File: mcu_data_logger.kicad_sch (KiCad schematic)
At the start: 25 parts, among them U1 24LC1025, U2 DS1337S_, U3 24LC1025, U4 ATMEGA328P-AU, Y1 32.768 kHz, Y2 16MHz

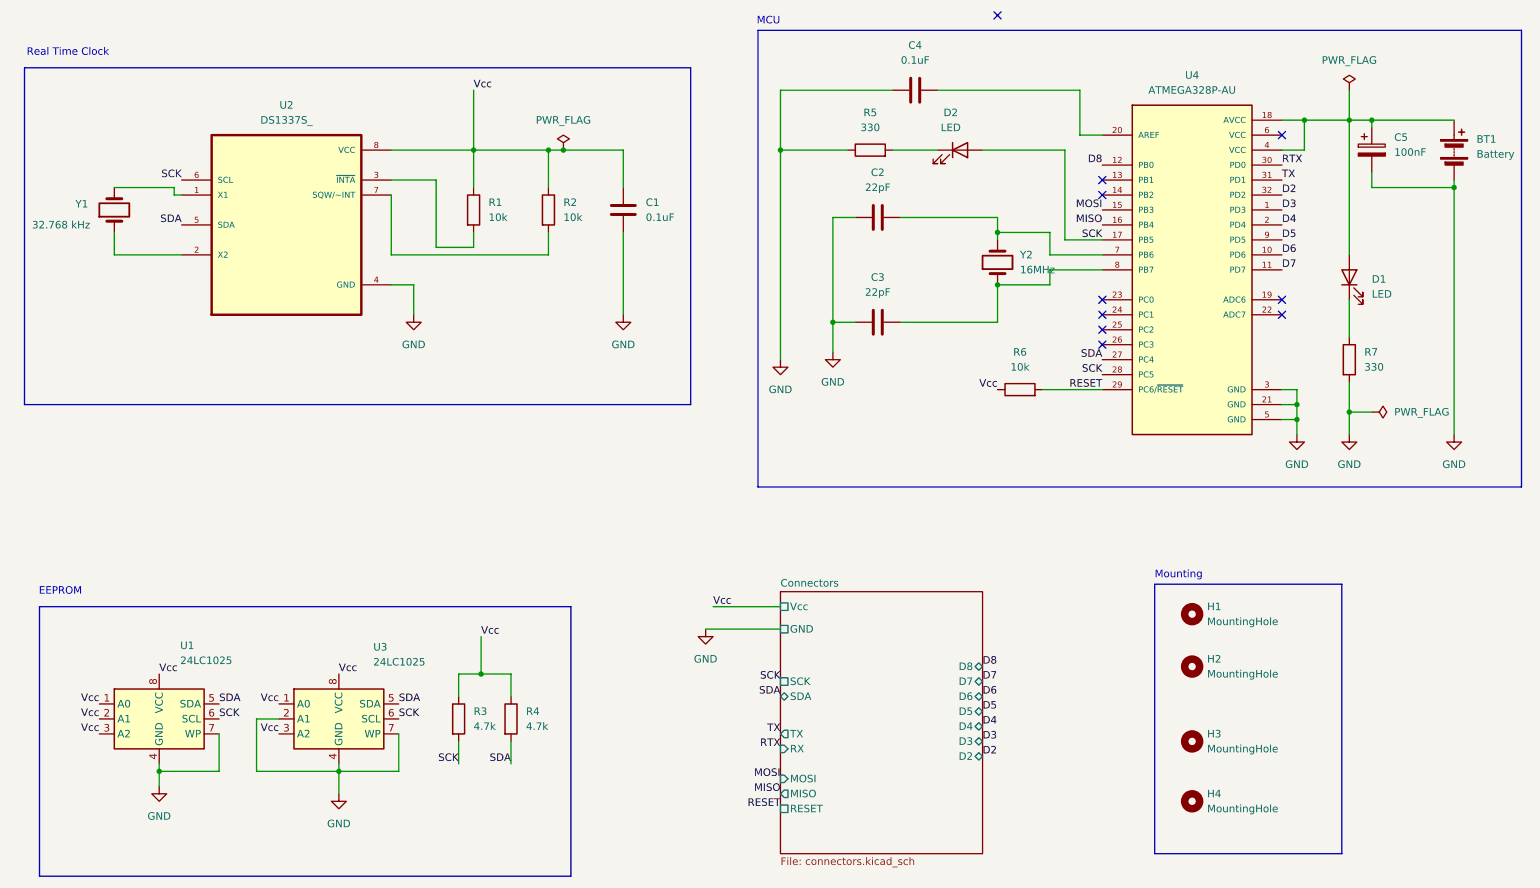
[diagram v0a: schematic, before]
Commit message: renamed RTX label from main sheet to RX
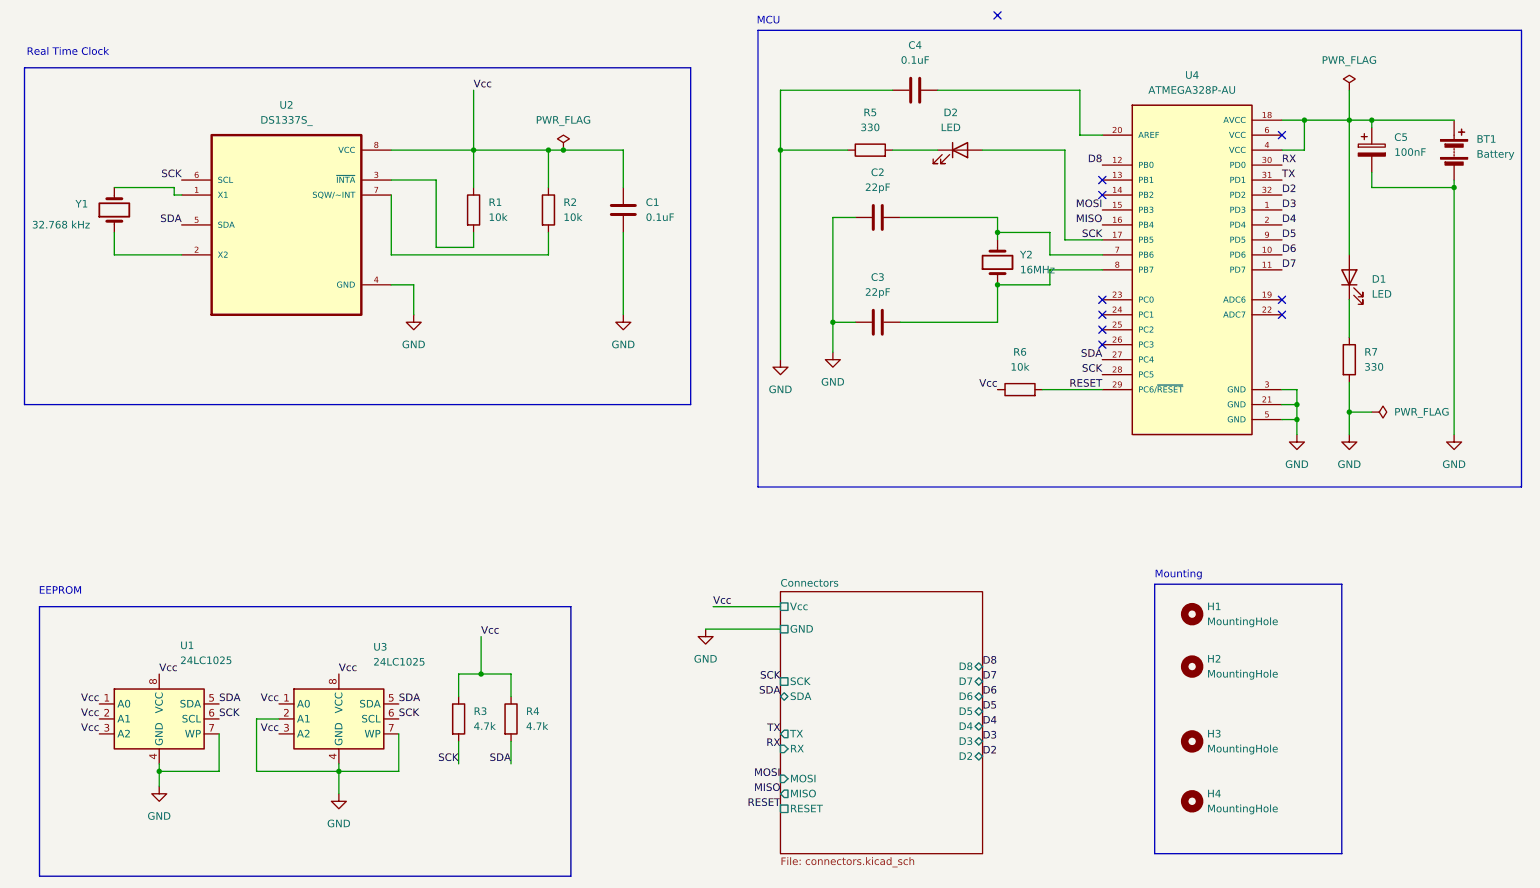
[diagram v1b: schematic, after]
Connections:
- net RTX renamed RX
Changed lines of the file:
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@@
 		)
 	)
-	(label "RTX"
+	(label "RX"
 		(at 157.48 142.24 180)
 		(effects
@@
 		)
 	)
-	(label "RTX"
+	(label "RX"
 		(at 242.57 43.18 0)
 		(effects

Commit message: Partial arrangement of footprints and change of battery component footprint
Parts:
- BT1: footprint Connector_PinHeader_2.54mm:PinHeader_1x02_P2.54mm_Horizontal -> Connector_PinHeader_2.54mm:PinHeader_1x02_P2.54mm_Vertical
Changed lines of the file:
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@@
 			)
 		)
-		(property "Footprint" "Connector_PinHeader_2.54mm:PinHeader_1x02_P2.54mm_Horizontal"
+		(property "Footprint" "Connector_PinHeader_2.54mm:PinHeader_1x02_P2.54mm_Vertical"
 			(at 271.78 39.116 90)
 			(effects

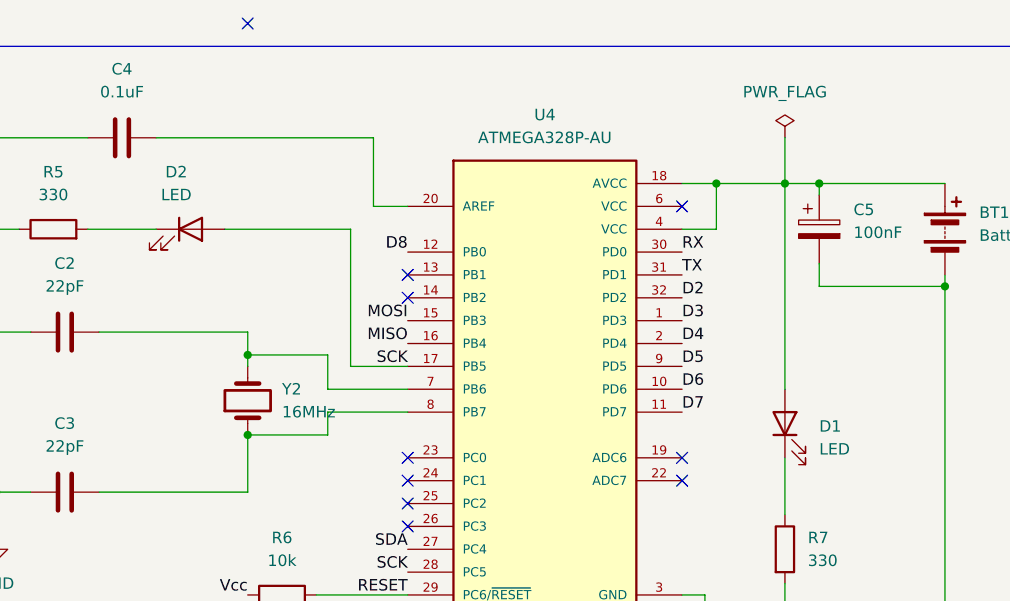
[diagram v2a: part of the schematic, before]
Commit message: swapped D1 and D2 diode references
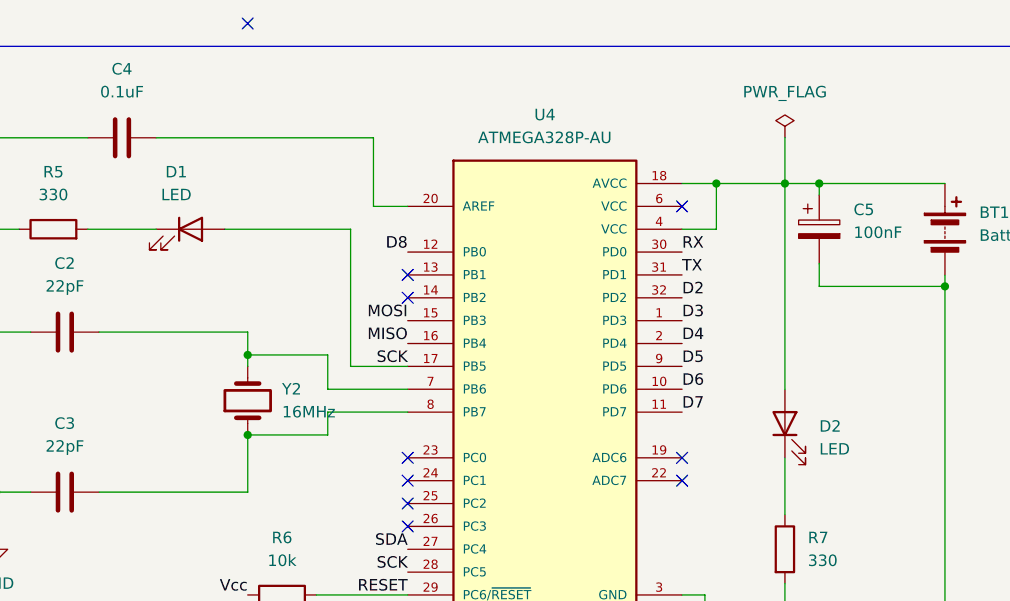
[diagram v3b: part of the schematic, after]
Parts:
- renumbered D2 to D1, D1 to D2
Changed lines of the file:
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@@
 		(dnp no)
 		(fields_autoplaced yes)
-		(property "Reference" "D2"
+		(property "Reference" "D1"
 			(at 186.3725 34.29 0)
 			(effects
@@
 			)
 		)
+		(property "Purpose" ""
+			(at 187.96 40.64 0)
+			(effects
+				(font
+					(size 1.27 1.27)
+				)
+			)
+		)
 		(pin "2"
 		)
@@
 			(project "mcu_data_logger"
 				(path "/8d241645-05dd-4180-8806-a9efe0716d11"
-					(reference "D2")
+					(reference "D1")
 					(unit 1)
 				)
@@
 		(dnp no)
 		(fields_autoplaced yes)
-		(property "Reference" "D1"
+		(property "Reference" "D2"
 			(at 257.81 62.5474 90)
 			(effects
@@
 			)
 		)
+		(property "Purpose" ""
+			(at 254 62.23 0)
+			(effects
+				(font
+					(size 1.27 1.27)
+				)
+			)
+		)
 		(pin "2"
 		)
@@
 			(project ""
 				(path "/8d241645-05dd-4180-8806-a9efe0716d11"
-					(reference "D1")
-					(unit 1)
-				)
+					(reference "D2")
+					(unit 1)
+				)

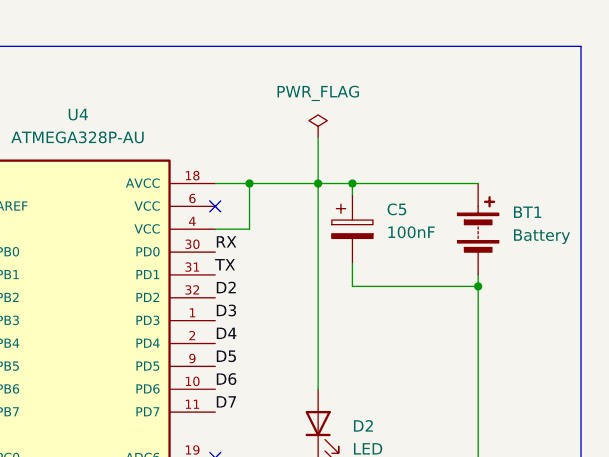
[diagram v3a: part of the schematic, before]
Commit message: assigned the Vcc net to the BT1 positive terminal in the Schematic Editor which resulted in a lot of bug fixing and rerouting in the PCB Editor
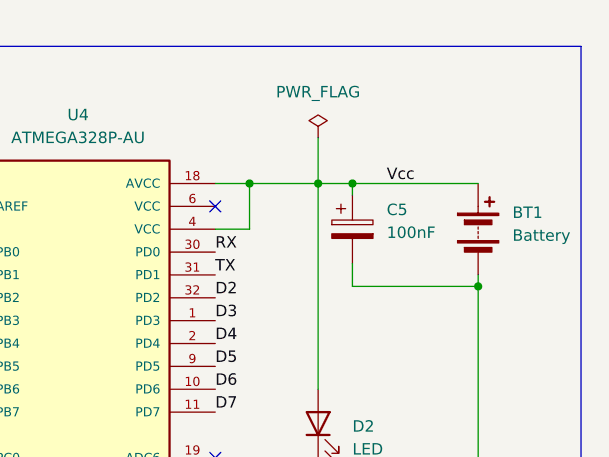
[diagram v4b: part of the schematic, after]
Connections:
- net Vcc: now also BT1.1 (+), C5.1, D2.2 (A), U4.18 (AVCC), U4.4 (VCC)
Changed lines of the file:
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@@
+		)
+	)
+	(label "Vcc"
+		(at 261.62 35.56 0)
+		(effects
+			(font
+				(size 1.27 1.27)
+			)
+			(justify left bottom)
 		)
 	)

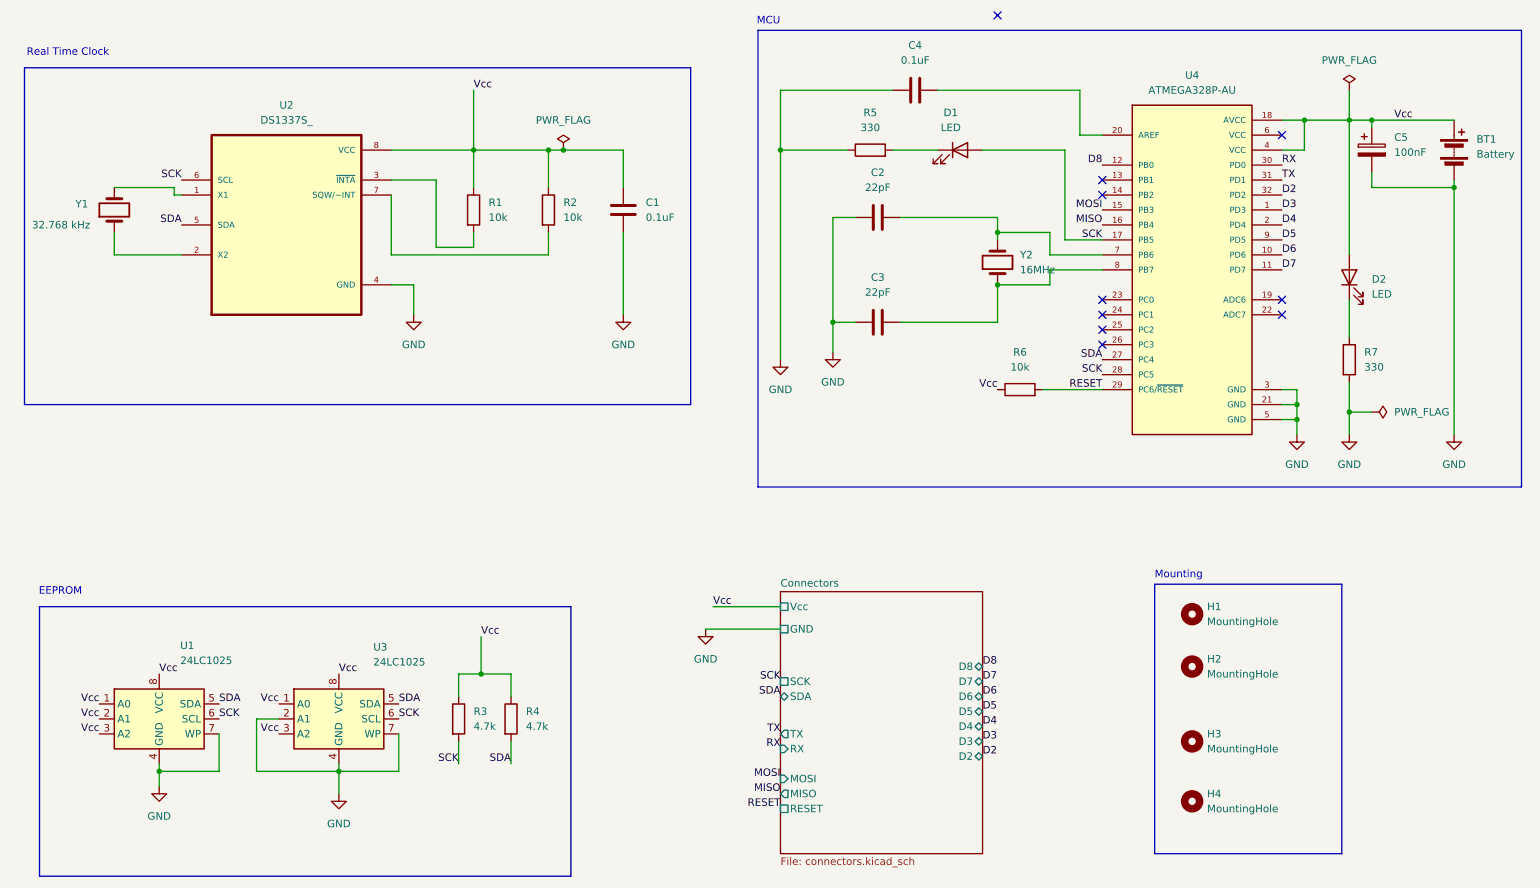
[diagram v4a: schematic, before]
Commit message: fixed net label bugs for i2c and icsp clock signal ports in the schematics
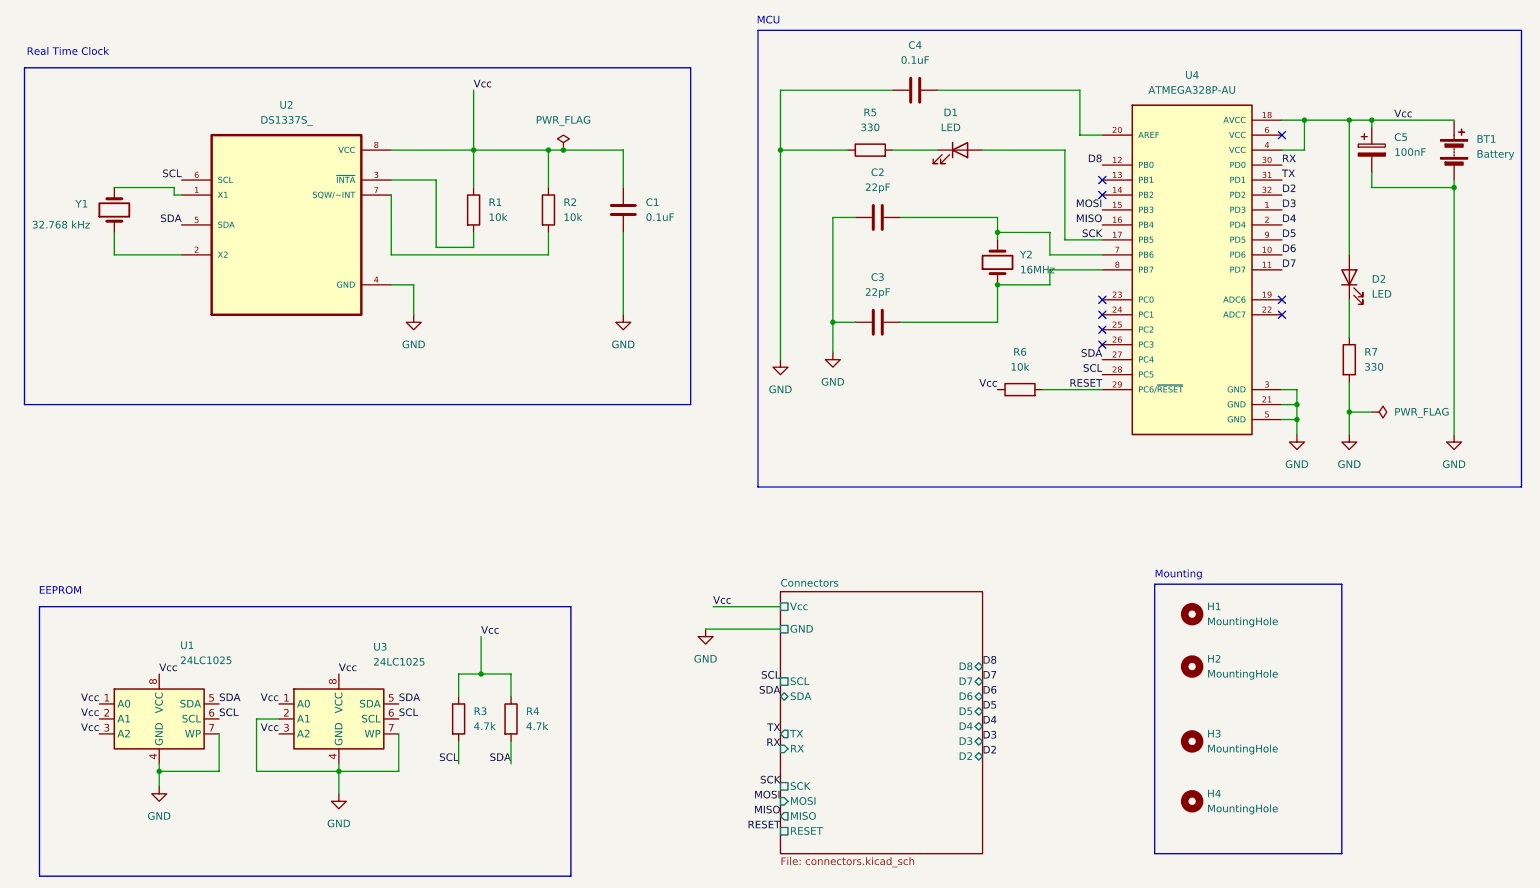
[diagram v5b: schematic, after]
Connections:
- net SCK: no longer R3.2, U1.6 (SCL), U2.6 (SCL), U3.6 (SCL), U4.28 (PC5)
- new net SCL: R3.2, U1.6 (SCL), U2.6 (SCL), U3.6 (SCL), U4.28 (PC5)
- no-connect marks 10 -> 9
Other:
- sheet Connectors ports: added SCL; removed none
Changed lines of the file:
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@@
 	)
 	(no_connect
-		(at 194.31 17.78)
-	)
-	(no_connect
 		(at 242.57 38.1)
 	)
@@
 	(wire
 		(pts
-			(xy 254 30.48) (xy 254 35.56)
-		)
-		(stroke
-			(width 0)
-			(type default)
-		)
-	)
-	(wire
-		(pts
 			(xy 212.09 60.96) (xy 203.2 60.96)
 		)
@@
 		)
 	)
-	(label "SCK"
+	(label "SCL"
 		(at 212.09 78.74 180)
 		(effects
@@
 		)
 	)
-	(label "SCK"
+	(label "SCL"
 		(at 102.87 144.78 180)
 		(effects
@@
 		)
 	)
-	(label "SCK"
+	(label "SCL"
 		(at 92.71 137.16 0)
 		(effects
@@
 	)
 	(label "MISO"
-		(at 157.48 149.86 180)
+		(at 157.48 153.67 180)
 		(effects
 			(font
@@
 		)
 	)
-	(label "SCK"
+	(label "SCL"
 		(at 62.23 137.16 0)
 		(effects
@@
 	)
 	(label "RESET"
-		(at 157.48 152.4 180)
+		(at 157.48 156.21 180)
 		(effects
 			(font
@@
 		)
 	)
-	(label "SCK"
+	(label "SCL"
 		(at 157.48 130.81 180)
 		(effects
@@
 		)
 	)
-	(label "SCK"
+	(label "SCL"
 		(at 55.88 45.72 180)
 		(effects
@@
 	)
 	(label "MOSI"
-		(at 157.48 147.32 180)
+		(at 157.48 151.13 180)
 		(effects
 			(font
@@
 		)
 	)
+	(label "SCK"
+		(at 157.48 148.59 180)
+		(effects
+			(font
+				(size 1.27 1.27)
+			)
+			(justify right bottom)
+		)
+	)
 	(symbol
 		(lib_id "Device:C")
@@
 	)
 	(symbol
-		(lib_id "power:PWR_FLAG")
-		(at 254 30.48 0)
-		(unit 1)
-		(exclude_from_sim no)
-		(in_bom yes)
-		(on_board yes)
-		(dnp no)
-		(fields_autoplaced yes)
-		(property "Reference" "#FLG01"
-			(at 254 28.575 0)
-			(effects
-				(font
-					(size 1.27 1.27)
-				)
-				(hide yes)
-			)
-		)
-		(property "Value" "PWR_FLAG"
-			(at 254 25.4 0)
-			(effects
-				(font
-					(size 1.27 1.27)
-				)
-			)
-		)
-		(property "Footprint" ""
-			(at 254 30.48 0)
-			(effects
-				(font
-					(size 1.27 1.27)
-				)
-				(hide yes)
-			)
-		)
-		(property "Datasheet" "~"
-			(at 254 30.48 0)
-			(effects
-				(font
-					(size 1.27 1.27)
-				)
-				(hide yes)
-			)
-		)
-		(property "Description" "Special symbol for telling ERC where power comes from"
-			(at 254 30.48 0)
-			(effects
-				(font
-					(size 1.27 1.27)
-				)
-				(hide yes)
-			)
-		)
-		(pin "1"
-		)
-		(instances
-			(project ""
-				(path "/8d241645-05dd-4180-8806-a9efe0716d11"
-					(reference "#FLG01")
-					(unit 1)
-				)
-			)
-		)
-	)
-	(symbol
 		(lib_id "Mechanical:MountingHole")
 		(at 227.33 128.27 0)
@@
 		)
 		(pin "MISO" output
-			(at 157.48 149.86 180)
+			(at 157.48 153.67 180)
 			(effects
 				(font
@@
 		)
 		(pin "RESET" passive
-			(at 157.48 152.4 180)
+			(at 157.48 156.21 180)
 			(effects
 				(font
@@
 			)
 		)
-		(pin "SCK" passive
-			(at 157.48 130.81 180)
-			(effects
-				(font
-					(size 1.27 1.27)
-				)
-				(justify left)
-			)
-		)
 		(pin "D4" bidirectional
 			(at 191.77 138.43 0)
@@
 		)
 		(pin "MOSI" input
-			(at 157.48 147.32 180)
+			(at 157.48 151.13 180)
 			(effects
 				(font
@@
 			(effects
 				(font
+					(size 1.27 1.27)
+				)
+				(justify left)
+			)
+		)
+		(pin "SCK" passive
+			(at 157.48 148.59 180)
+			(effects
+				(font
+					(size 1.27 1.27)
+				)
+				(justify left)
+			)
+		)
+		(pin "SCL" passive
+			(at 157.48 130.81 180)
+			(effects
+				(font
